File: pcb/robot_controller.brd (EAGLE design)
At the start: 139 x 90 mm, 93 parts, among them IC2 ESP32-DEVKIT, IC3 BTS7960B, IC4 BTS7960B, IC5 BTS7960B, IC6 BTS7960B, IC7 BTS7960B, IC8 BTS7960B, J6 1X2-3.5MM, Q1 IRLB8743

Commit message: update PCB to v1.1
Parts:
- added C43: (no value), rcl:E5-10,5
- C42: value 10nF -> 100nF
- moved C42 77.0 mm to (202.5, -55.0)
- moved R20 73.9 mm to (202.5, -52.5), turned to 180 degrees
- moved R18 63.8 mm to (197.5, -55.0), turned to 180 degrees
- moved R16 8.78 mm to (280.5, -50.0), turned to 0 degrees
- moved JP1 5.00 mm to (288.5, -69.0)
- moved C18 3.50 mm to (193.0, -27.5)
- moved D4 0.50 mm to (196.0, -29.5)
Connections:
- removed net A13: IC2.28
- removed net N$8: IC2.25
- net GND: now also C43.-
- net VBATT: now also C43.+
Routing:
- net N$79: track 0.00 -> 58.1 mm, vias 0 -> 4
- net N$15: track 31.0 -> 45.4 mm
- net VBATT: track 196.8 -> 198.8 mm
- net GND: track 0.00 -> 1.32 mm, vias 163 -> 169
- net N$27: track 6.33 -> 7.46 mm
- net N$9: vias 21 -> 22
- net N$6: vias 5 -> 19
- net N$5: vias 5 -> 20
- net N$4: vias 5 -> 22
- net N$2: vias 5 -> 21
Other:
- board text added: "Robot controller v1.1 - dec 2022"

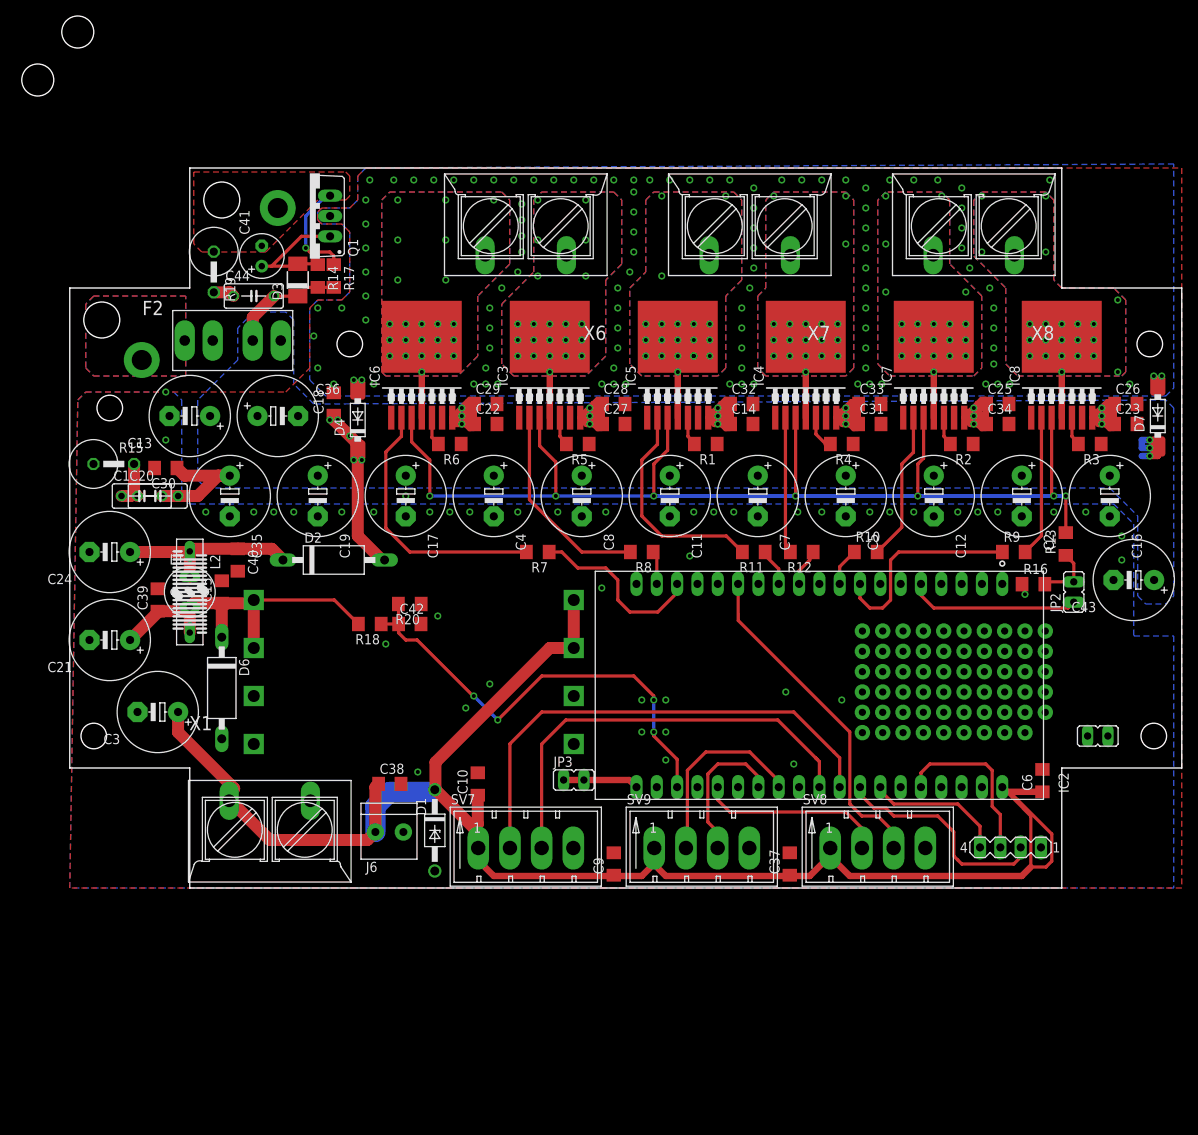
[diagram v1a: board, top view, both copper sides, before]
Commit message: update PCB and gerbers for v1.1
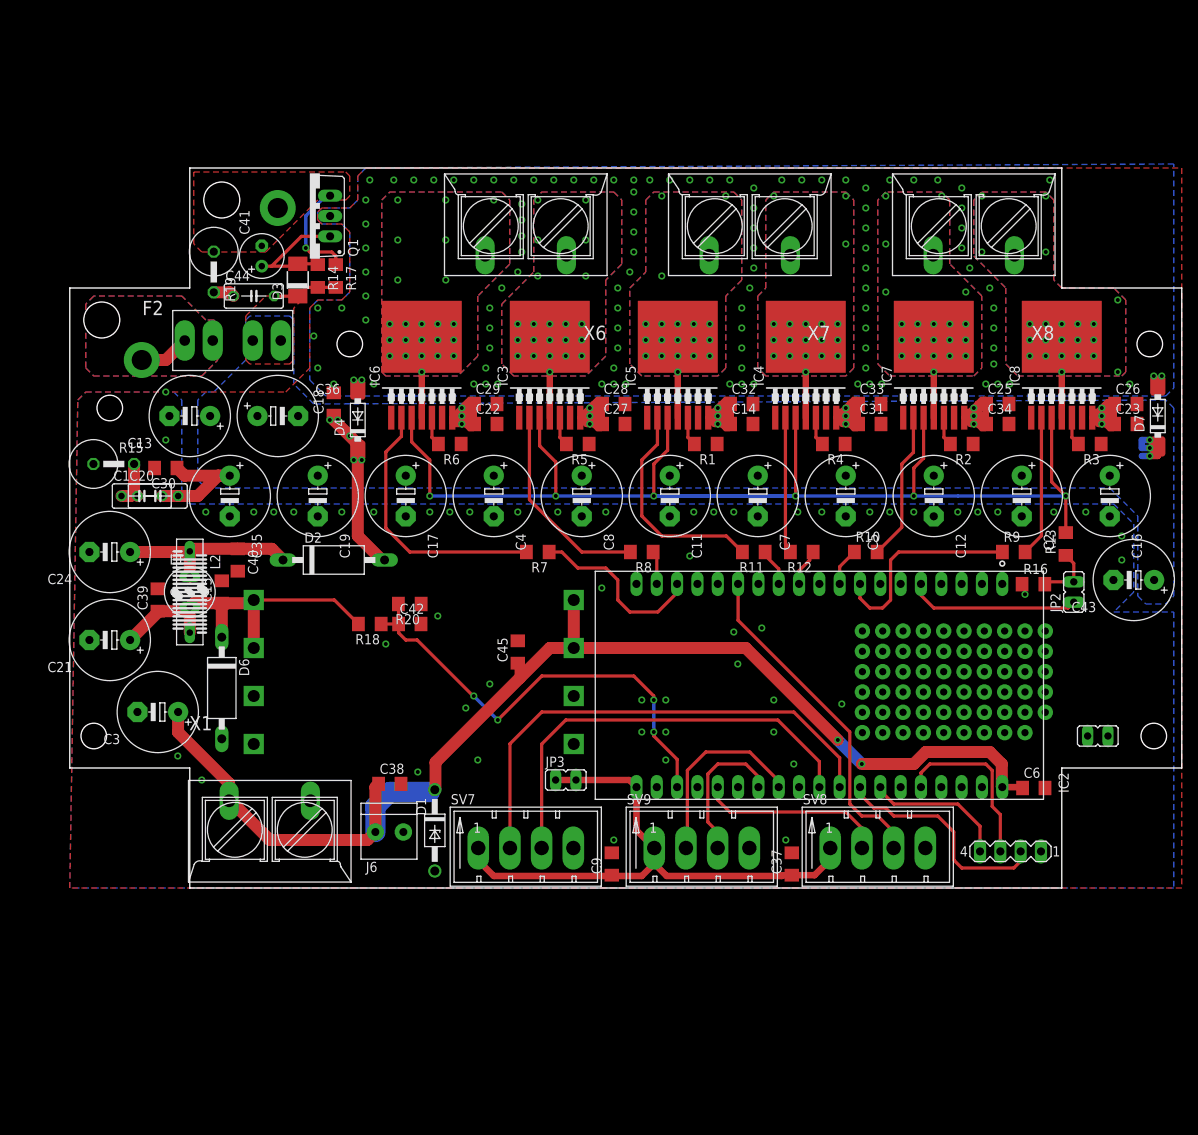
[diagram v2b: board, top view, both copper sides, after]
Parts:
- removed C10: (no value), rcl:C1206
- added C45: (no value), rcl:C1206
- moved C6 1.42 mm to (280.5, -75.5), turned to 0 degrees
- moved JP3 1.00 mm to (222.0, -74.5)
- moved R4 1.00 mm to (255.5, -32.5)
- moved SV6 0.50 mm to (277.6, -83.4)
- moved C37 0.25 mm to (250.2, -85.0)
- moved C9 0.25 mm to (227.8, -85.0)
- moved R17 0.25 mm to (193.2, -11.5)
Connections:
- net +3V3: now also C37.1, C9.1, SV7.1, SV8.1, SV9.1
- net +5V: now also C45.1; no longer C10.1, C37.1, C9.1, SV7.1, SV8.1, SV9.1
- net GND: now also C45.2; no longer C10.2
- net N$7: now also F2.1B
- net VBATT: now also F2.2B
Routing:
- net N$18: track 247.6 -> 164.3 mm, vias 7 -> 6
- net +3V3: track 9.48 -> 70.9 mm
- net +5V: track 208.7 -> 152.1 mm, vias 0 -> 2
- net N$7: track 0.00 -> 6.54 mm
- net VBATT: track 198.8 -> 193.4 mm
- net GND: track 1.32 -> 0.00 mm, vias 169 -> 177
- net N$14: track 4.38 -> 3.63 mm
- net SPI_SCLK: track 27.9 -> 28.4 mm
- net SPI_MOSI: track 21.5 -> 22.0 mm
- net SPI_MISO: track 17.4 -> 17.9 mm
- net N$5: vias 20 -> 19
- added copper zone on layer 1, net VBATT

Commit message: add jumpers to the PCB for setting the address
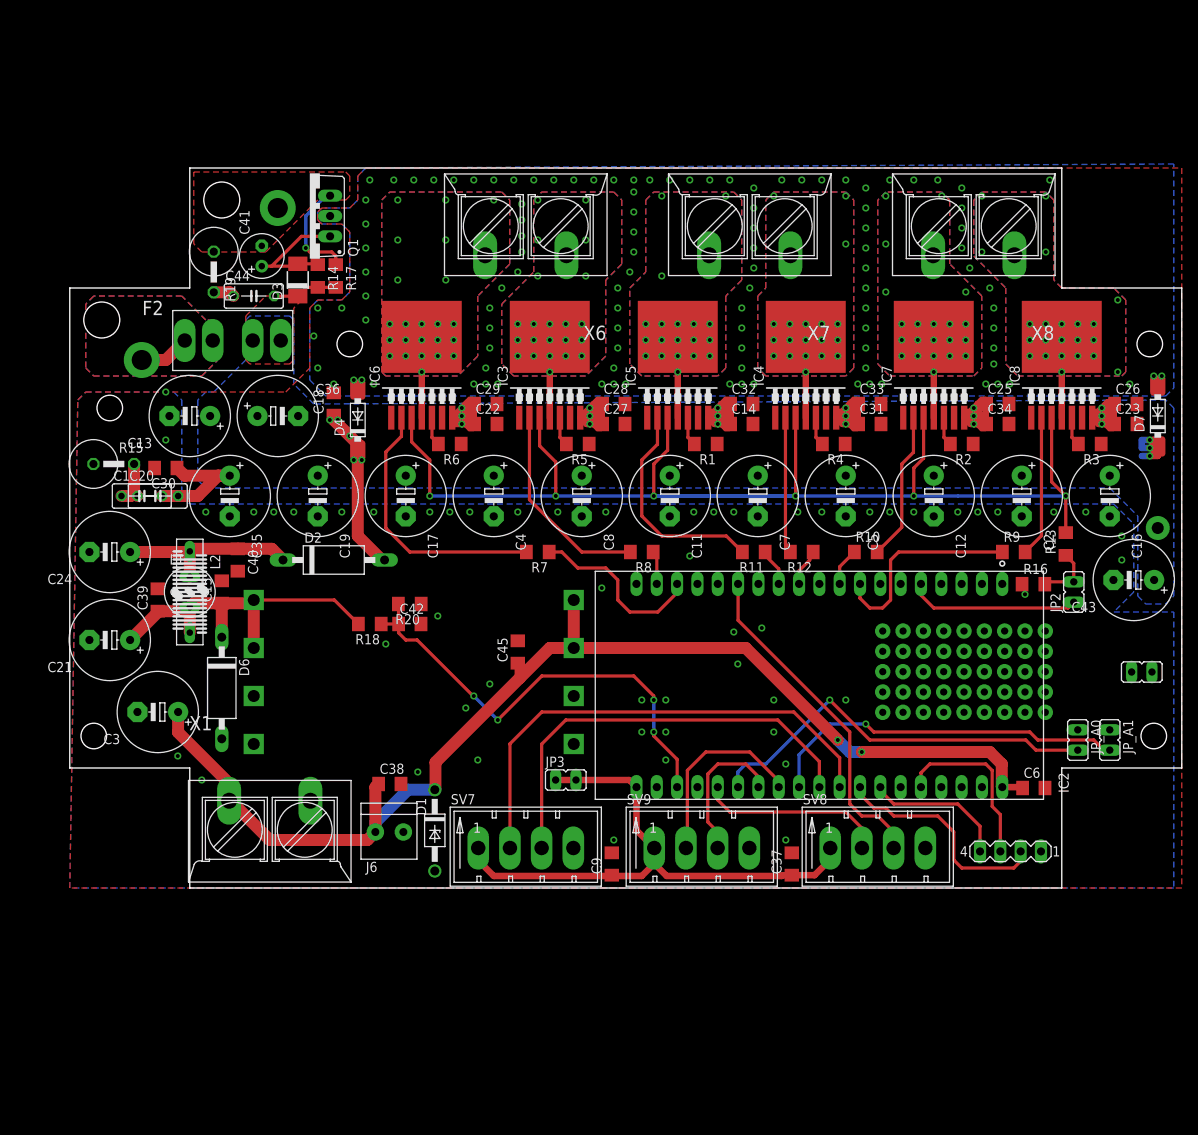
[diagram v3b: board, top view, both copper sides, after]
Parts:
- added JP_A0, JP_A1: (no value), jumper:JP1
- moved JP1 9.71 mm to (294.0, -61.0)
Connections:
- new net N$29: IC2.25, JP_A0.2
- new net N$8: IC2.28, JP_A1.2
- net GND: now also JP_A0.1, JP_A1.1
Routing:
- net N$29: track 0.00 -> 50.7 mm, vias 0 -> 1
- net N$8: track 0.00 -> 45.8 mm, vias 0 -> 1
- net +5V: track 152.1 -> 149.7 mm
- net VBATT: vias 26 -> 27
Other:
- board text added: "A0"
- board text added: "A1"
- board text added: "ENABLE"
- board text added: "MOTORS"
- board text added: "Robot controller v1.2 - feb 2023"
- board text added: "VBATT"
- board text removed: "ENABLE MOTORS"
- board text removed: "Robot controller v1.1 - dec 2022"

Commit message: add GND and +12V tap points to the controller PCB
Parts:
- removed C20: (no value), rcl:C050-030X075
- added C10: (no value), rcl:C1206
- added JP4: M01PTH_LONGPAD, SparkFun:1X01_LONGPAD
- C1: device rcl:C050-030X075 -> rcl:C025-025X050
- R15: device rcl:0617V -> rcl:0411V
- moved C30 6.04 mm to (166.5, -33.0)
- moved C1 4.24 mm to (172.0, -42.0)
- moved R15 3.54 mm to (166.0, -38.5)
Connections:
- net GND: now also C10.2
- net N$26: no longer C20.1
- net VBATT: now also C10.1, JP4.1; no longer C20.2
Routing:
- net N$26: track 5.93 -> 4.93 mm
- net VBATT: track 193.4 -> 193.7 mm, vias 27 -> 29
- net N$10: vias 23 -> 22
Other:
- board text added: "+12V"
- board text added: "Robot controller v1.3 - Jul 2023"
- board text removed: "Robot controller v1.2 - feb 2023"
- board text removed: "VBATT"
